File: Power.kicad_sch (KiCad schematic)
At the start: 30 parts

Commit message: working on power again with new compoenets
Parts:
- removed C? (x4): 22muF, symbol Device:C_Small
- removed L?: 470nH, symbol Device:L
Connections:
- net at U?.25 (SW_B0): no longer U?.26 (SW_B0)
- net 1V8: no longer names the net of U?.2 (FB_B0)
- net AWR_MCUCLKOUT: no longer names the net of U?.7 (WDI)
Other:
- moved on the sheet: U?

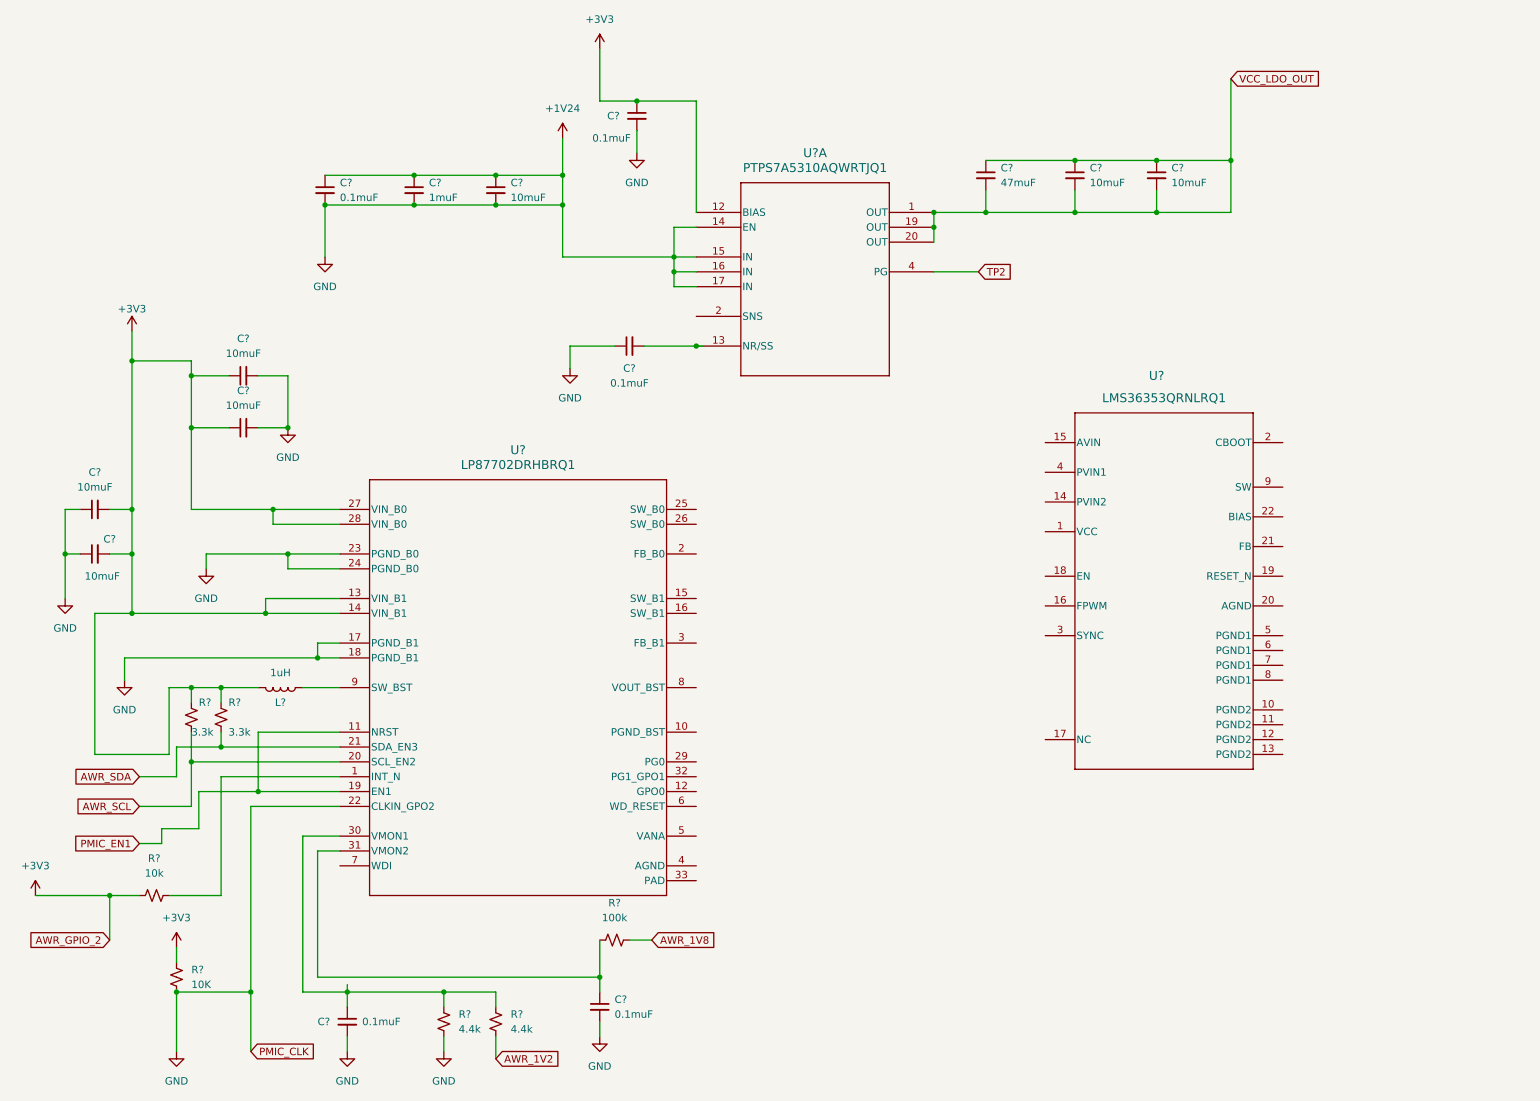
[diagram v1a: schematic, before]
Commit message: finished BQ charge controller
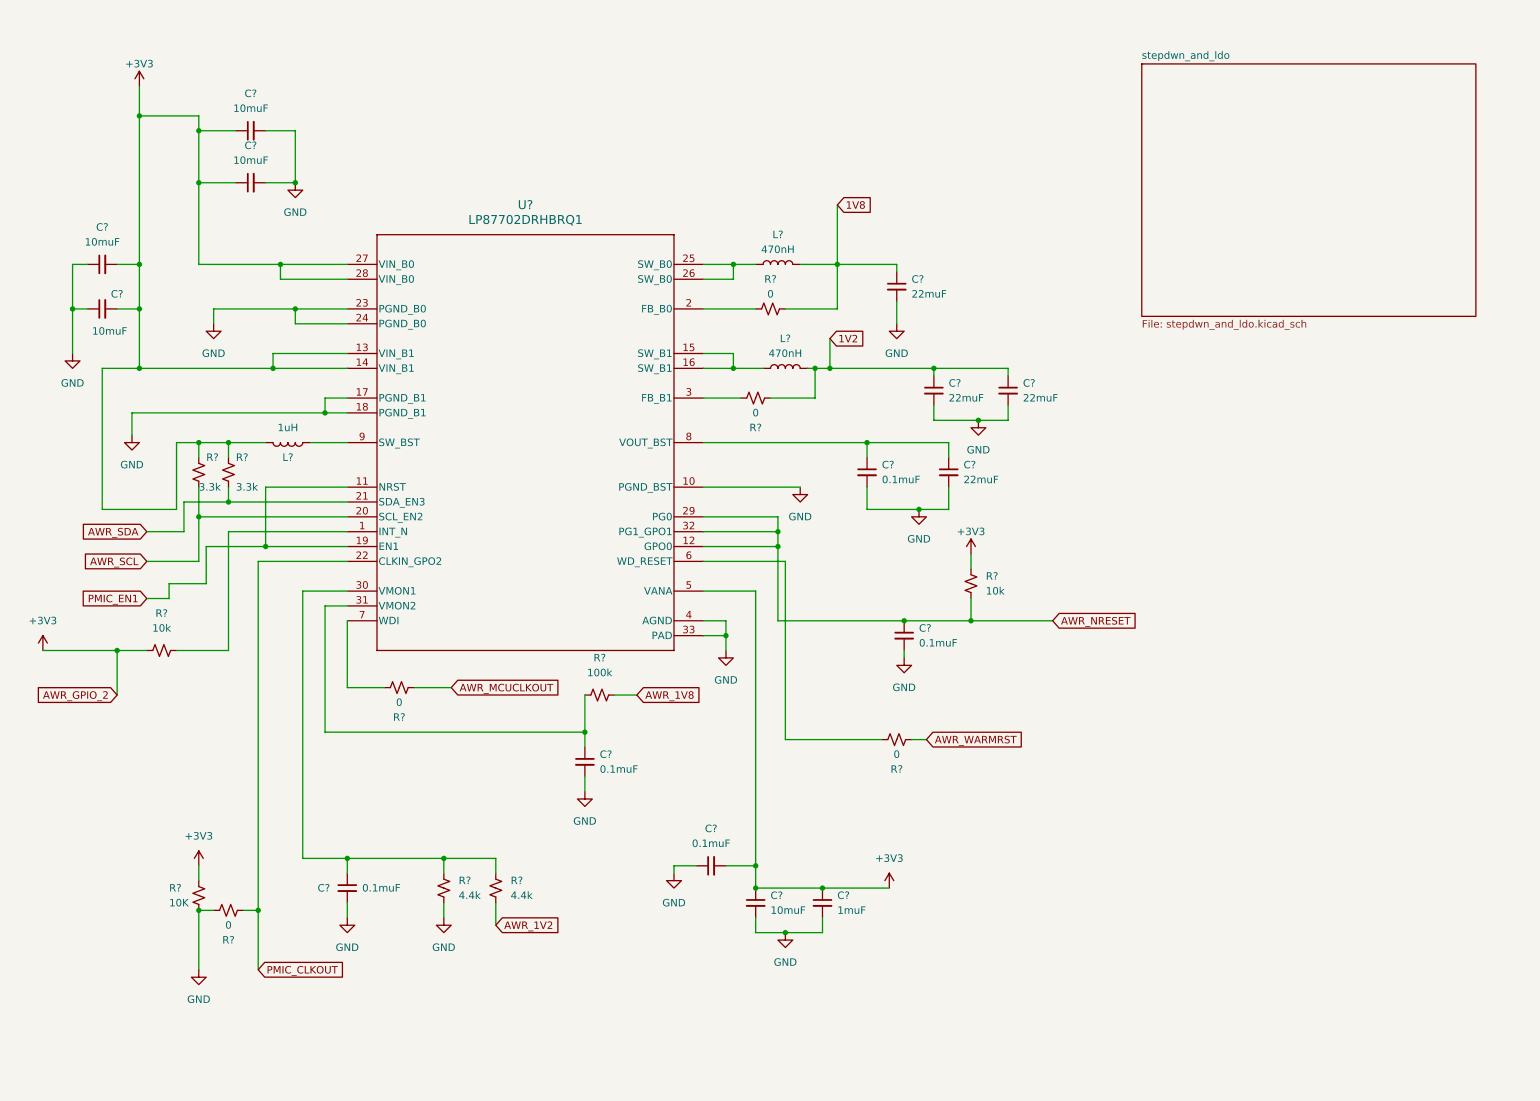
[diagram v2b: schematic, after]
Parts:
- removed C? (x3): 10muF, symbol Device:C_Small
- removed C? (x3): 0.1muF, symbol Device:C_Small
- removed C?: 1muF, symbol Device:C_Small
- removed C?: 47muF, symbol Device:C_Small
- removed U?: LMS36353QRNLRQ1, RNL0022A, symbol LMS3635-Q1:LMS36353QRNLRQ1
- removed U?: PTPS7A5310AQWRTJQ1, WQFN20_RTJ_TEX, symbol TPS7A5301QRGRRQ1:PTPS7A5310AQWRTJQ1
- added C? (x4): 22muF, symbol Device:C_Small
- added C? (x3): 0.1muF, symbol Device:C_Small
- added C?: 10muF, symbol Device:C_Small
- added C?: 1muF, symbol Device:C_Small
- added L? (x2): 470nH, symbol Device:L
- added R? (x5): 0, symbol Device:R_Small_US
- added R?: 10k, symbol Device:R_Small_US
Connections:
- net +3V3: now also U?.5 (VANA), C?.1, C?.1, C?.2, R?.1
- net GND: now reaches U?.10 (PGND_BST)
- net GND: now also C?.1, C?.1, C?.2, C?.2, C?.2, C?.2, R?.2, R?.2, U?.17 (PGND_B1), U?.18 (PGND_B1), U?.23 (PGND_B0), U?.24 (PGND_B0), U?.33 (PAD), U?.4 (AGND), C?.1, C?.2, C?.2, C?.2, C?.2, C?.2, C?.2, C?.2, C?.2, R?.2
- net AWR_NRESET: now reaches U?.12 (GPO0)
- net AWR_NRESET: now also U?.29 (PG0), U?.32 (PG1_GPO1), C?.1, R?.2
- net at U?.15 (SW_B1): now also U?.16 (SW_B1), L?.1
- net at U?.2 (FB_B0): now also R?.1
- net at U?.25 (SW_B0): now also U?.26 (SW_B0), L?.1
- net at U?.3 (FB_B1): now also R?.2
- net at U?.6 (WD_RESET): now also R?.2
- net at U?.7 (WDI): now also R?.2
- net at U?.8 (VOUT_BST): now also C?.1, C?.1
- removed net +1V35: C?.1, C?.1, C?.2, C?.2, C?.2, C?.2, R?.2, R?.2, U?.17 (PGND_B1), U?.18 (PGND_B1), U?.22 (CLKIN_GPO2), U?.23 (PGND_B0), U?.24 (PGND_B0)
- new net 1V2: C?.1, C?.1, L?.2, R?.1
- new net 1V8: C?.1, L?.2, R?.2
- new net AWR_MCUCLKOUT: R?.1
- new net AWR_WARMRST: R?.1
- new net PMIC_CLKOUT: R?.1, U?.22 (CLKIN_GPO2)
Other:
- added sheet stepdwn_and_ldo (stepdwn_and_ldo.kicad_sch)
- moved on the sheet: C?, L?, R?, U?

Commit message: squased errors going over supply desgin
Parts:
- added R26, R27: 0, symbol Device:R_Small_US
- gave numbers to parts that had none: 32
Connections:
- net AWR_NRESET: now also R26.2, R27.2; no longer U1.12 (GPO0), U1.29 (PG0), U1.32 (PG1_GPO1)
- net 5VBST: now reaches C26.1, C30.1, U1.8 (VOUT_BST)
- new net: R27.1, U1.12 (GPO0)
- new net: R26.1, U1.29 (PG0)
- no-connect marks 0 -> 1
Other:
- moved on the sheet: C30

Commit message: working on connectors
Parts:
- L1: value 1uH -> 1muH
- L2, L3: value 470nH -> 0.47muH
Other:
- note added: "note frm datasheet: Use ceramic capacitors, X7R or X7T types; do not use Y5V or F"
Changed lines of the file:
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@@
     (stroke (width 0) (type default))
+  )
+  (text "note frm datasheet:\nUse ceramic capacitors, X7R or X7T types; \ndo not use Y5V or F"
+    (at 142.24 36.83 0)
+    (effects (font (size 1.27 1.27)) (justify left bottom))
   )
   (global_label "PMIC_EN1" (shape input) (at 41.91 113.03 180) (fields_autoplaced)
@@
       (effects (font (size 1.27 1.27)))
     )
-    (property "Value" "470nH" (at 151.13 71.12 90)
+    (property "Value" "0.47muH" (at 151.13 71.12 90)
       (effects (font (size 1.27 1.27)))
     )
@@
       (effects (font (size 1.27 1.27)))
     )
-    (property "Value" "1uH" (at 66.04 83.82 90)
+    (property "Value" "1muH" (at 66.04 83.82 90)
       (effects (font (size 1.27 1.27)))
     )
@@
       (effects (font (size 1.27 1.27)))
     )
-    (property "Value" "470nH" (at 149.86 53.34 90)
-      (effects (font (size 1.27 1.27)))
-    )
+    (property "Value" "0.47muH" (at 149.86 53.34 90)
+      (effects (font (size 1.27 1.27)))
+    )
